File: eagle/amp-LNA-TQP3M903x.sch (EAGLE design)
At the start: 18 parts, among them J1 142-0701-851, J2 142-0701-851, U1 TQP3M903X

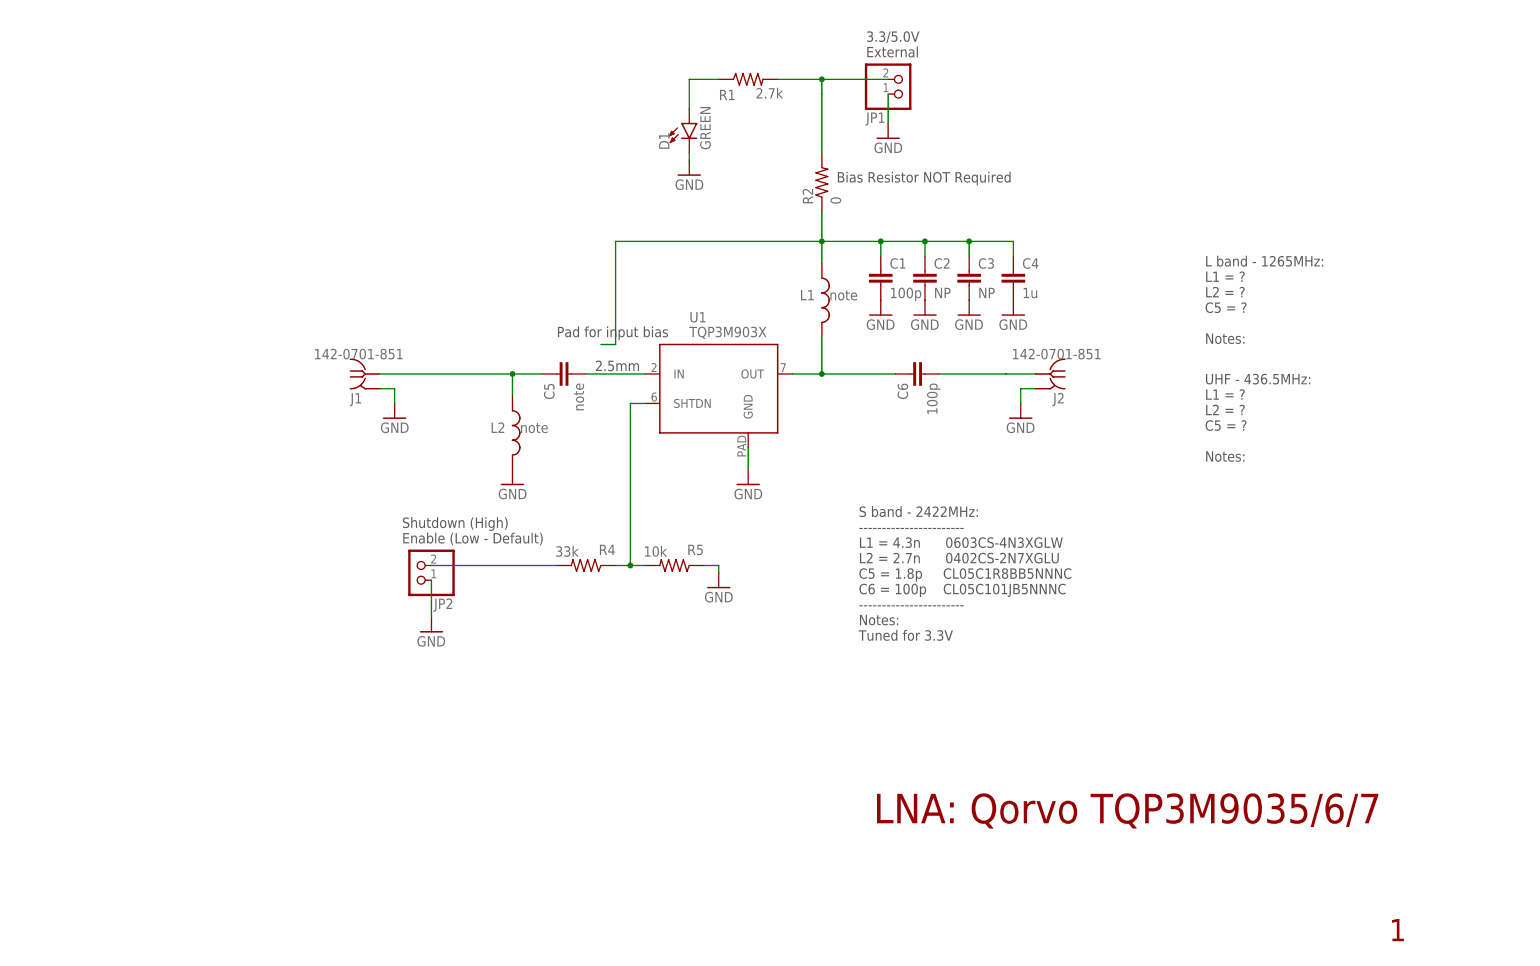
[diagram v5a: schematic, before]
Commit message: Add optional choke, and organize
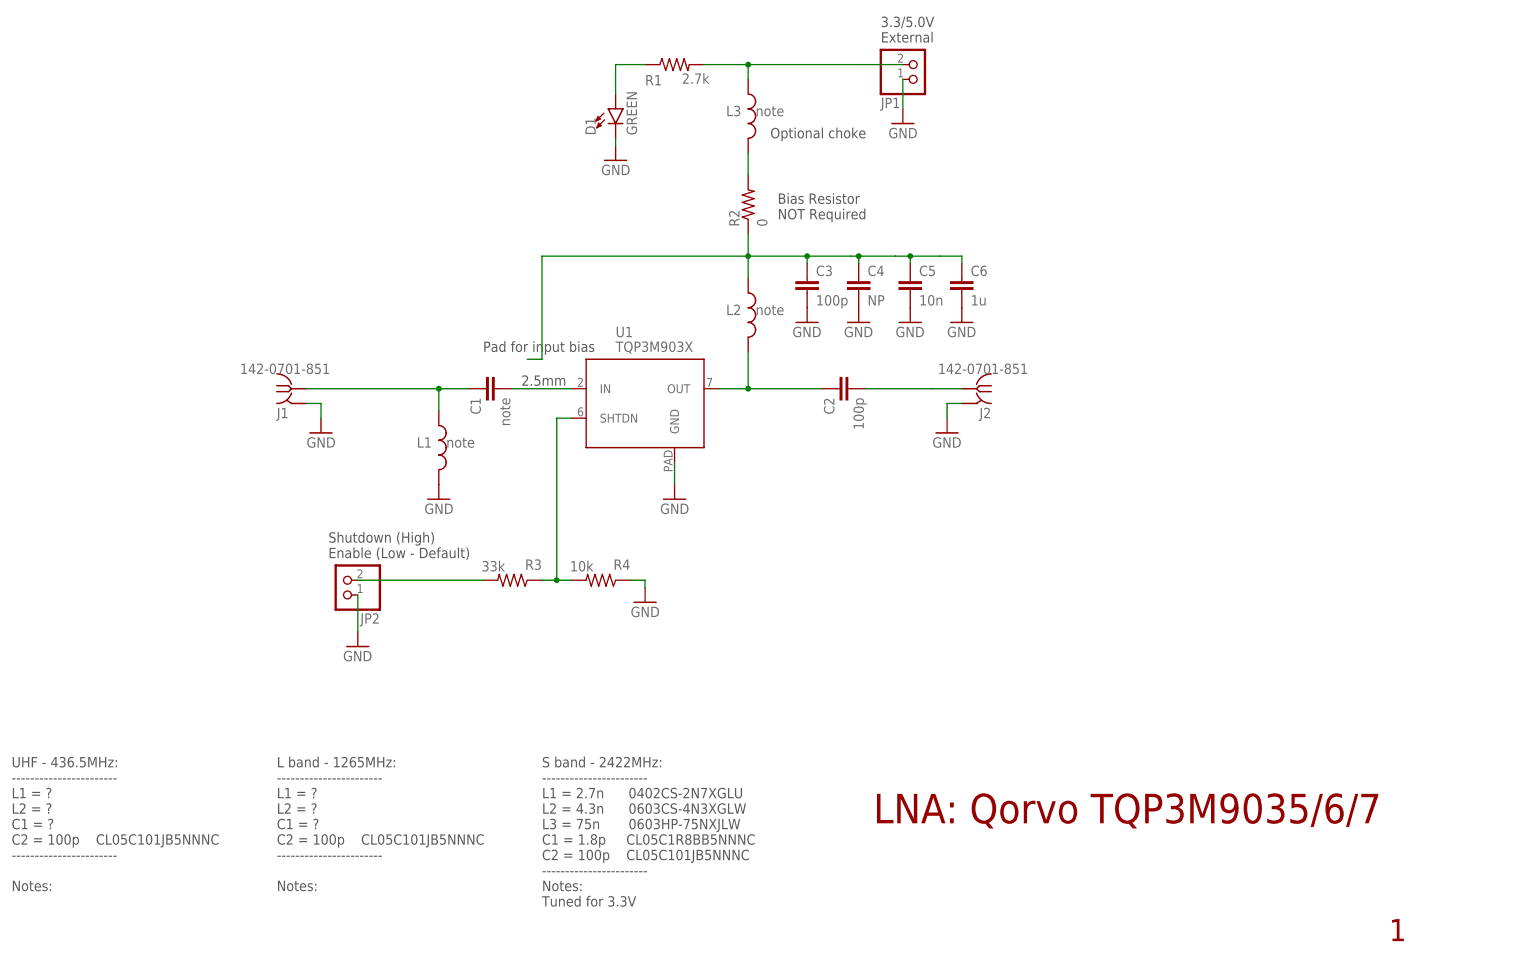
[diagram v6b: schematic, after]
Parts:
- removed R5: 10k, oresat-rcl:R-US_0603-B-NOSILK
- added L3: note, oresat-rcl:L-US0603-B-NOSILK
- added R3: 33k, oresat-rcl:R-US_0603-B-NOSILK
- C1: value 100p -> note; device oresat-rcl:C-EU0603-B-NOSILK -> oresat-rcl:C-EU0402-C-NOSILK
- C2: value NP -> 100p; device oresat-rcl:C-EU0603-B-NOSILK -> oresat-rcl:C-EU0402-C-NOSILK
- C3: value NP -> 100p
- C4: value 1u -> NP
- C5: value note -> 10n; device oresat-rcl:C-EU0402-C-NOSILK -> oresat-rcl:C-EU0603-B-NOSILK
- C6: value 100p -> 1u; device oresat-rcl:C-EU0402-C-NOSILK -> oresat-rcl:C-EU0603-B-NOSILK
- L1: device oresat-rcl:L-US0603-C-NOSILK -> oresat-rcl:L-US0402-C-NOSILK
- L2: device oresat-rcl:L-US0402-C-NOSILK -> oresat-rcl:L-US0603-C-NOSILK
- R2: device oresat-rcl:R-US_0805-B-NOSILK -> oresat-rcl:R-US_0603-B-NOSILK
- R4: value 33k -> 10k
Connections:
- new net N$5: L3.2, R2.2
- net GND: now also C5.2, C6.2, L1.2, R4.1; no longer C1.2, C2.2, L2.2, R5.1
- net N$1: now also L3.1; no longer R2.2
- net N$2: now also R3.1, R4.2; no longer R4.1, R5.2
- net N$28: now also C2.1, L2.2; no longer C6.1, L1.2
- net N$3: now also R3.2; no longer R4.2
- net N$4: now also C1.2; no longer C5.2
- net N$47: now also C5.1, C6.1, L2.1; no longer C1.1, C2.1, L1.1
- net RF_IN: now also C1.1, L1.1; no longer C5.1, L2.1
- net RF_OUT: now also C2.2; no longer C6.2
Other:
- note added: "L band - 1265MHz: ----------------------- L1 = ? L2 = ? C1 = ? C2 = 100p CL05C101JB5NNNC ----------------------- Notes:"
- note added: "Optional choke"
- note added: "S band - 2422MHz: ----------------------- L1 = 2.7n 0402CS-2N7XGLU L2 = 4.3n 0603CS-4N3XGLW L3 = 75n 0603HP-75NXJLW C1 = 1.8p CL05C1R8BB5NNNC C2 = 100p CL05C101JB5NNNC ----------------------- Notes: Tuned for 3.3V"
- note added: "UHF - 436.5MHz: ----------------------- L1 = ? L2 = ? C1 = ? C2 = 100p CL05C101JB5NNNC ----------------------- Notes:"
- note removed: "L band - 1265MHz: L1 = ? L2 = ? C5 = ? Notes:"
- note removed: "S band - 2422MHz: ----------------------- L1 = 4.3n 0603CS-4N3XGLW L2 = 2.7n 0402CS-2N7XGLU C5 = 1.8p CL05C1R8BB5NNNC C6 = 100p CL05C101JB5NNNC ----------------------- Notes: Tuned for 3.3V"
- note removed: "UHF - 436.5MHz: L1 = ? L2 = ? C5 = ? Notes:"
- moved on the sheet: C1, C2, C3, C4, C5, C6, D1, J1, J2, JP1, JP2, L1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
